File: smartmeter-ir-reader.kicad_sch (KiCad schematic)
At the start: 0 parts

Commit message: Initial version
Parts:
- added C1, C2, C3: 1uF, Capacitor_SMD:C_0603_1608Metric_Pad1.08x0.95mm_HandSolder, symbol Device:C
- added D1: BAT46W, Diode_SMD:D_SOD-123, symbol Device:D_Schottky
- added D2: LED, LED_THT:LED_D3.0mm_Clear, symbol Device:LED
- added IC1, IC2: SN74LVC1G17DBVR, Chof747 Footprints:SOT95P270X145-5N, symbol Chof747 ICs:SN74LVC1G17DBVR
- added J1: RJ10, Connector_RJ:RJ12_Amphenol_54601, symbol Connector:RJ10
- added Q1: S8050, Package_TO_SOT_SMD:SOT-23, symbol Transistor_BJT:S8050
- added Q2: S8550, Package_TO_SOT_SMD:SOT-23, symbol Transistor_BJT:S8550
- added Q3: SFH309, LED_THT:LED_D3.0mm_Clear, symbol Sensor_Optical:SFH309
- added R1, R2, R3: 10k, Resistor_SMD:R_0603_1608Metric_Pad0.98x0.95mm_HandSolder, symbol Device:R
- added R4: 180, Resistor_SMD:R_0603_1608Metric_Pad0.98x0.95mm_HandSolder, symbol Device:R
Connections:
- new net: IC2.4 (Y), R3.1
- new net: Q2.2 (B), R3.2
- new net: Q1.2 (B), Q3.2 (E), R2.1
- new net: IC1.2 (A), Q1.3 (C), R1.2
- new net: D2.2 (A), Q2.3 (C)
- new net: D2.1 (K), R4.2
- new net +3V3: C1.1, C2.1, C3.1, D1.1 (K), IC1.5 (VCC), IC2.5 (VCC), Q2.1 (E), Q3.1 (C), R1.1
- new net GND: C1.2, C2.2, C3.2, IC1.3 (GND), IC2.3 (GND), J1.1, Q1.1 (E), R2.2, R4.1
- new net RX: IC1.4 (Y), J1.2
- new net TX: IC2.2 (A), J1.3
- new net VCC: D1.2 (A), J1.4

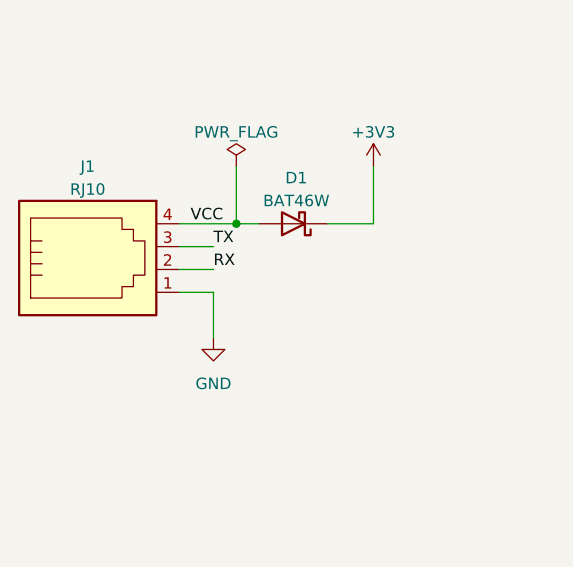
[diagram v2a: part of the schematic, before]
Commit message: corrected RJ12 socket Connector
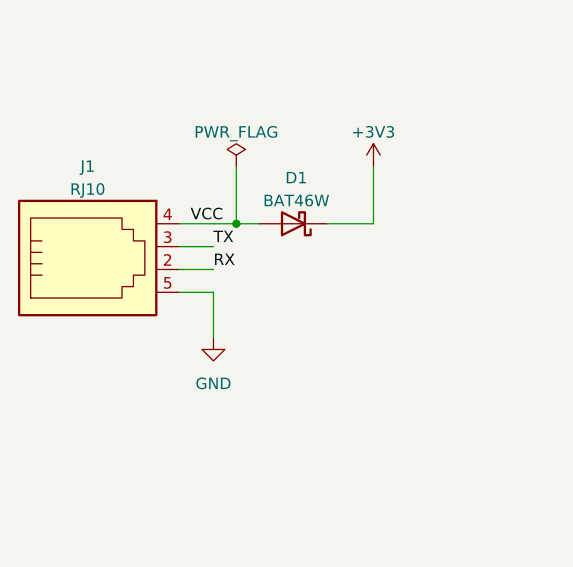
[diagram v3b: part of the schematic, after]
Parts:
- J1: symbol Connector:RJ10 -> Chof747 Connectors:RJ12
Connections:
- net GND: now also J1.5; no longer J1.1
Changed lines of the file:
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@@
     )
   )
-  (symbol (lib_id "Connector:RJ10") (at 46.99 53.34 0) (unit 1)
+  (symbol (lib_id "Chof747 Connectors:RJ12") (at 46.99 53.34 0) (unit 1)
     (in_bom yes) (on_board yes) (dnp no) (fields_autoplaced)
     (property "Reference" "J1" (at 46.99 41.91 0)
@@
       (effects (font (size 1.27 1.27)) hide)
     )
-    (pin "1")
     (pin "2")
     (pin "3")
     (pin "4")
+    (pin "5")
     (instances
       (project "smartmeter-ir-reader"

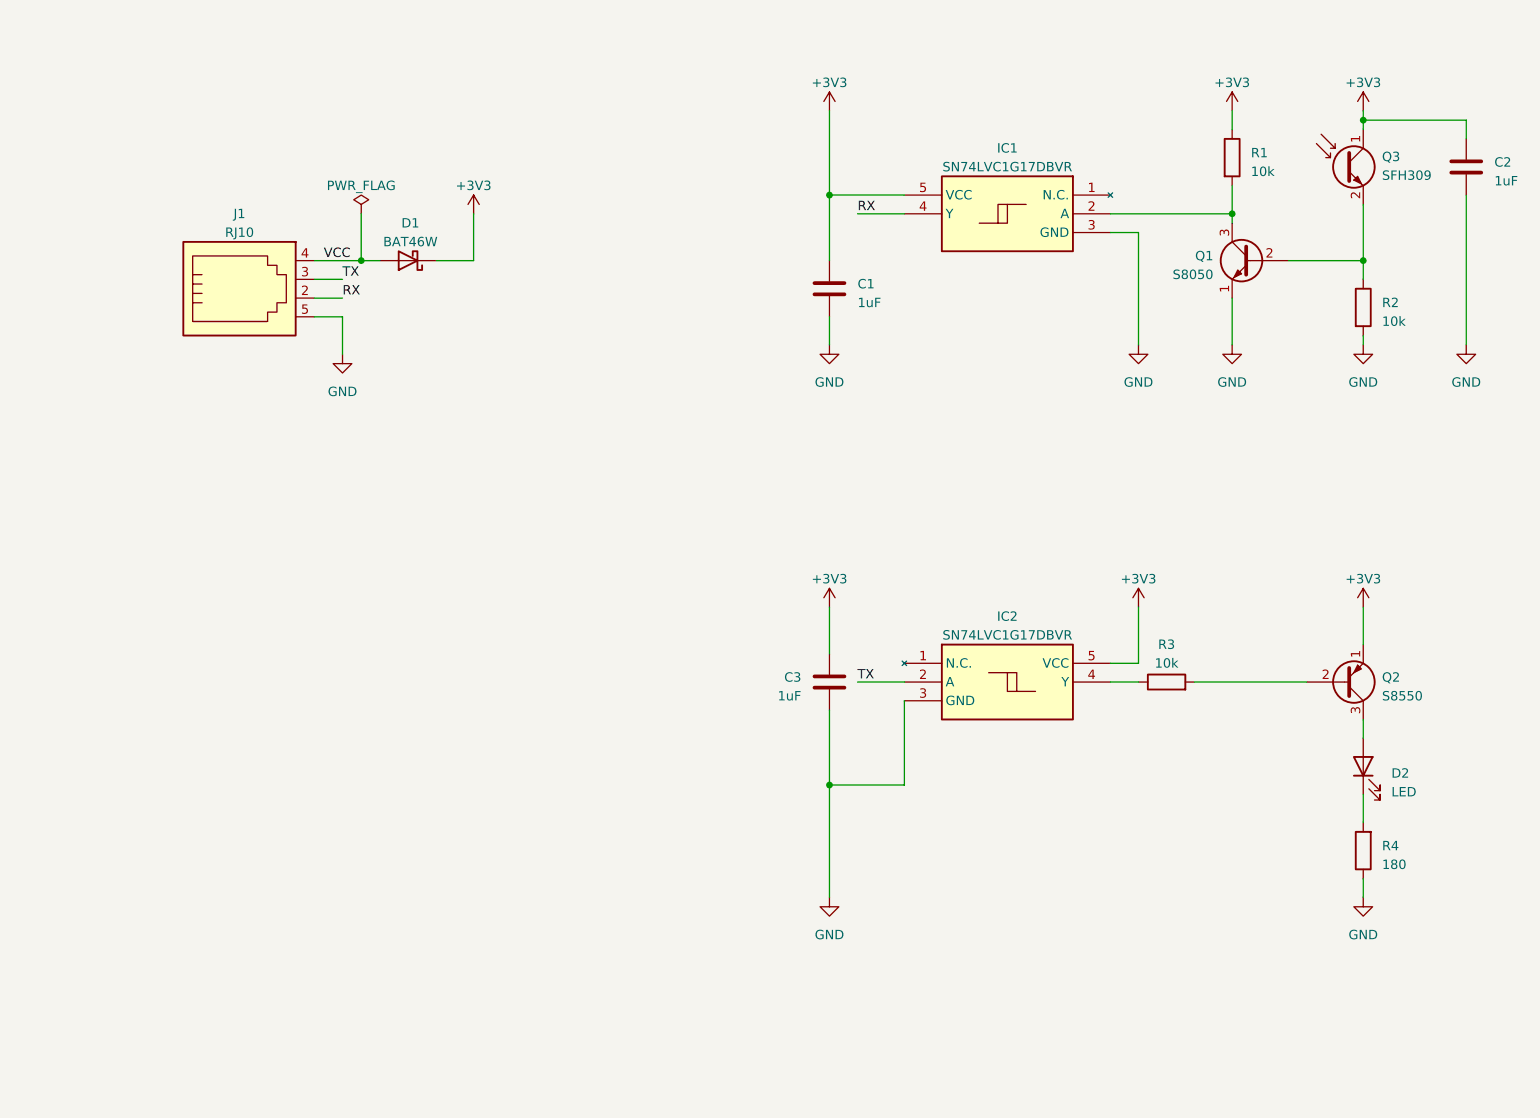
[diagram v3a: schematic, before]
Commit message: Reformatted schematic
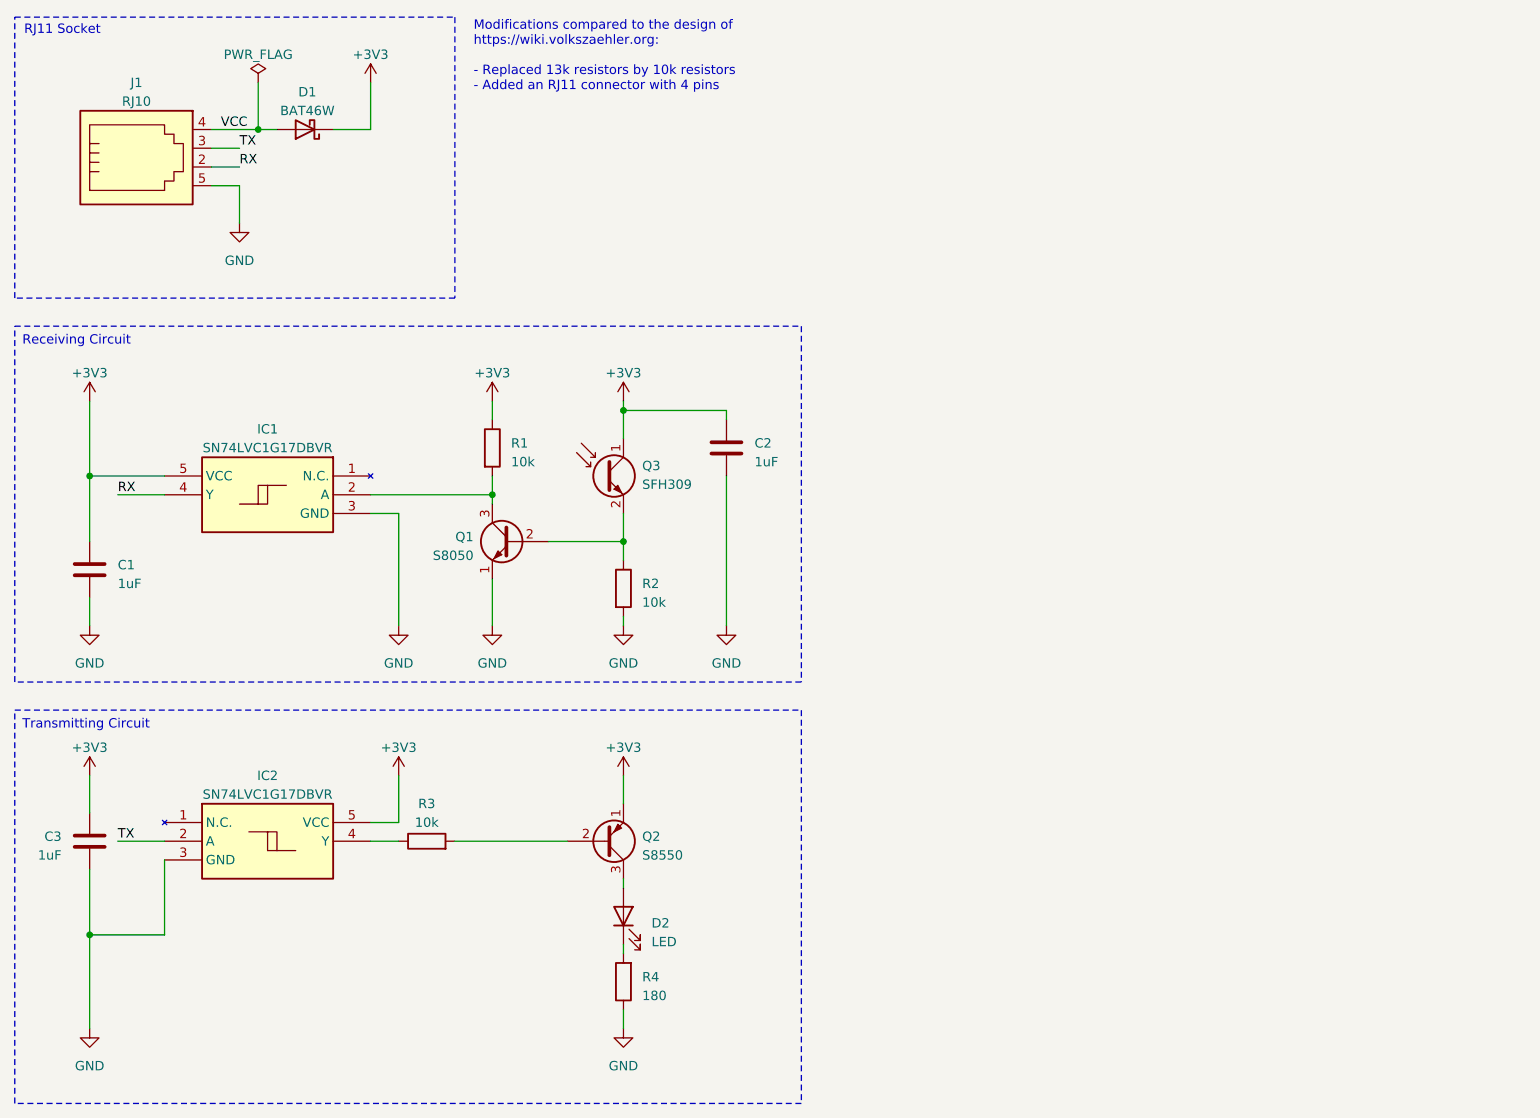
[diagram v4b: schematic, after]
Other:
- note added: "Modifications compared to the design of https://wiki.volkszaehler.org: - Replaced 13k resistors by 10k resistors - Added an RJ11 connector with 4 pins"
- note added: "RJ11 Socket"
- title: (none) -> Smartmeter IR Read/Write Connector
- moved on the sheet: C1, C2, C3, D1, D2, IC1, IC2, J1, Q1, Q2, Q3, R1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

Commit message: V1.2 with corrected transistor layouts
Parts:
- removed Q1: S8050, Package_TO_SOT_SMD:SOT-23, symbol Transistor_BJT:S8050
- added Q1: SS8050-G, Package_TO_SOT_SMD:SOT-23, symbol Device:Q_NPN_BEC
- Q2: symbol Transistor_BJT:S8550 -> Device:Q_PNP_BEC
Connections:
- net +3V3: now also Q2.2 (E); no longer Q2.1 (E)
- net GND: now also Q1.2 (E)
- net at R3.2: now also Q2.1 (B); no longer Q2.2 (B)
- net at Q3.2 (E), R2.1: now also Q1.1 (B)
- net at IC1.2 (A), R1.2: now also Q1.3 (C)
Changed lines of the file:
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@@
+    )
+  )
+  (symbol (lib_id "Device:Q_NPN_BEC") (at 83.82 86.36 0) (mirror y) (unit 1)
+    (in_bom yes) (on_board yes) (dnp no)
+    (property "Reference" "Q1" (at 78.74 85.0899 0)
+      (effects (font (size 1.27 1.27)) (justify left))
+    )
+    (property "Value" "SS8050-G" (at 92.71 91.44 0)
+      (effects (font (size 1.27 1.27)) (justify left))
+    )
+    (property "Footprint" "Package_TO_SOT_SMD:SOT-23" (at 78.74 83.82 0)
+      (effects (font (size 1.27 1.27)) hide)
+    )
+    (property "Datasheet" "~" (at 83.82 86.36 0)
+      (effects (font (size 1.27 1.27)) hide)
+    )
+    (pin "1")
+    (pin "2")
+    (pin "3")
+    (instances
+      (project "smartmeter-ir-reader"
+        (path "/e8426e51-e5a9-4642-8277-6d3f50e0e523"
+          (reference "Q1") (unit 1)
+        )
+      )
     )
   )
@@
         (path "/e8426e51-e5a9-4642-8277-6d3f50e0e523"
           (reference "#PWR06") (unit 1)
-        )
-      )
-    )
-  )
-  (symbol (lib_id "Transistor_BJT:S8050") (at 83.82 86.36 0) (mirror y) (unit 1)
-    (in_bom yes) (on_board yes) (dnp no)
-    (property "Reference" "Q1" (at 78.74 85.725 0)
-      (effects (font (size 1.27 1.27)) (justify left))
-    )
-    (property "Value" "S8050" (at 78.74 88.265 0)
-      (effects (font (size 1.27 1.27)) (justify left))
-    )
-    (property "Footprint" "Package_TO_SOT_SMD:SOT-23" (at 78.74 88.265 0)
-      (effects (font (size 1.27 1.27) italic) (justify left) hide)
-    )
-    (property "Datasheet" "http://www.unisonic.com.tw/datasheet/S8050.pdf" (at 83.82 86.36 0)
-      (effects (font (size 1.27 1.27)) (justify left) hide)
-    )
-    (pin "1")
-    (pin "2")
-    (pin "3")
-    (instances
-      (project "smartmeter-ir-reader"
-        (path "/e8426e51-e5a9-4642-8277-6d3f50e0e523"
-          (reference "Q1") (unit 1)
         )
       )
@@
     )
   )
-  (symbol (lib_id "Transistor_BJT:S8550") (at 96.52 127 0) (mirror x) (unit 1)
+  (symbol (lib_id "Device:Q_PNP_BEC") (at 96.52 127 0) (mirror x) (unit 1)
     (in_bom yes) (on_board yes) (dnp no)
     (property "Reference" "Q2" (at 101.6 126.365 0)
@@
       (effects (font (size 1.27 1.27)) (justify left))
     )
-    (property "Footprint" "Package_TO_SOT_SMD:SOT-23" (at 101.6 125.095 0)
-      (effects (font (size 1.27 1.27) italic) (justify left) hide)
-    )
-    (property "Datasheet" "http://www.unisonic.com.tw/datasheet/S8550.pdf" (at 96.52 127 0)
-      (effects (font (size 1.27 1.27)) (justify left) hide)
-    )
-    (pin "1")
+    (property "Footprint" "Package_TO_SOT_SMD:SOT-23" (at 101.6 129.54 0)
+      (effects (font (size 1.27 1.27)) hide)
+    )
+    (property "Datasheet" "~" (at 96.52 127 0)
+      (effects (font (size 1.27 1.27)) hide)
+    )
+    (pin "1")
